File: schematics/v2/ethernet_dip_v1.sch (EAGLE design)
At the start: 30 parts

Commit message: added eeprom
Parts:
- added IC2: DS2432P, 1wire:DS2432P
- added R10: (no value), rcl:R-EU_R0805
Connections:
- net GND: now also IC2P.GND
- net LD2: now also IC2_1W.1W, R10.1
- net VDD: now also R10.2
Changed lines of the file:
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@@
 <part name="GND11" library="supply1" deviceset="GND" device=""/>
 <part name="SUPPLY6" library="SparkFun-Aesthetics" deviceset="VDD" device="" value="+3.3v"/>
+<part name="IC2" library="1wire" deviceset="DS2432" device="P"/>
+<part name="GND14" library="supply1" deviceset="GND" device=""/>
+<part name="R10" library="rcl" deviceset="R-EU_" device="R0805"/>
+<part name="SUPPLY7" library="SparkFun-Aesthetics" deviceset="VDD" device="" value="+3.3v"/>
 </parts>
 <sheets>
@@
 <instance part="GND11" gate="1" x="247.65" y="209.55"/>
 <instance part="SUPPLY6" gate="VDD" x="279.4" y="215.9"/>
+<instance part="IC2" gate="G$1" x="304.8" y="127"/>
+<instance part="IC2" gate="P" x="312.42" y="116.84" rot="R270"/>
+<instance part="IC2" gate="_1W" x="309.88" y="119.38"/>
+<instance part="GND14" gate="1" x="302.26" y="111.76"/>
+<instance part="R10" gate="G$1" x="289.56" y="127" rot="R90"/>
+<instance part="SUPPLY7" gate="VDD" x="289.56" y="134.62"/>
 </instances>
 <busses>
@@
 <wire x1="241.3" y1="213.36" x2="241.3" y2="205.74" width="0.1524" layer="91"/>
 </segment>
+<segment>
+<pinref part="IC2" gate="P" pin="GND"/>
+<pinref part="GND14" gate="1" pin="GND"/>
+<wire x1="304.8" y1="116.84" x2="302.26" y2="116.84" width="0.1524" layer="91"/>
+<wire x1="302.26" y1="116.84" x2="302.26" y2="114.3" width="0.1524" layer="91"/>
+</segment>
 </net>
 <net name="INT0" class="0">
@@
 <wire x1="299.72" y1="198.12" x2="287.02" y2="198.12" width="0.1524" layer="91"/>
 <label x="289.56" y="198.12" size="1.778" layer="95"/>
+</segment>
+<segment>
+<pinref part="IC2" gate="_1W" pin="1W"/>
+<label x="294.64" y="119.38" size="1.778" layer="95"/>
+<wire x1="304.8" y1="119.38" x2="289.56" y2="119.38" width="0.1524" layer="91"/>
+<pinref part="R10" gate="G$1" pin="1"/>
+<wire x1="289.56" y1="119.38" x2="284.48" y2="119.38" width="0.1524" layer="91"/>
+<wire x1="289.56" y1="121.92" x2="289.56" y2="119.38" width="0.1524" layer="91"/>
+<junction x="289.56" y="119.38"/>
 </segment>
 </net>
@@
 <wire x1="279.4" y1="213.36" x2="279.4" y2="215.9" width="0.1524" layer="91"/>
 </segment>
-</net>
+<segment>
+<pinref part="R10" gate="G$1" pin="2"/>
+<wire x1="289.56" y1="134.62" x2="289.56" y2="132.08" width="0.1524" layer="91"/>
+<pinref part="SUPPLY7" gate="VDD" pin="VDD"/>
+</segment>
+</net>

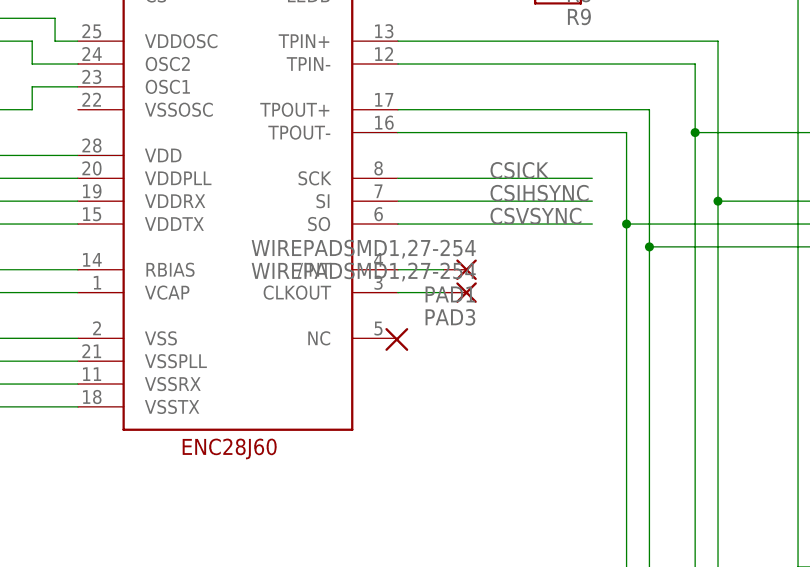
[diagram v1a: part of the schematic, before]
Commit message: routed interrupt pin
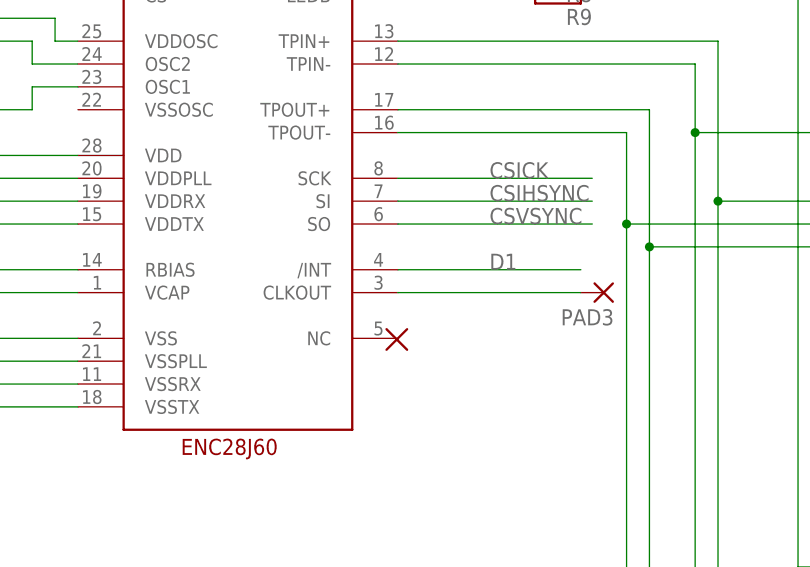
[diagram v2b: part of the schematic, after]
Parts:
- removed PAD1: WIREPADSMD1,27-254, wirepad:WIREPADSMD1,27-254
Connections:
- removed net N$12: PAD1.P, U1./INT
- net D1: now also U1./INT
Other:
- moved on the sheet: PAD3
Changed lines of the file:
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@@
 <part name="C8" library="rcl" deviceset="C-EU" device="C0805"/>
 <part name="GND3" library="supply1" deviceset="GND" device=""/>
-<part name="PAD1" library="wirepad" deviceset="WIREPAD" device="SMD1,27-254"/>
 <part name="PAD3" library="wirepad" deviceset="WIREPAD" device="SMD1,27-254"/>
 <part name="R4" library="rcl" deviceset="R-EU_" device="R0805"/>
@@
 <instance part="C8" gate="G$1" x="41.91" y="165.1" rot="R180"/>
 <instance part="GND3" gate="1" x="241.3" y="139.7"/>
-<instance part="PAD1" gate="G$1" x="116.84" y="172.72" rot="R180"/>
-<instance part="PAD3" gate="G$1" x="116.84" y="170.18" rot="R180"/>
+<instance part="PAD3" gate="G$1" x="132.08" y="170.18" smashed="yes" rot="R180">
+<attribute name="NAME" x="133.223" y="168.3258" size="1.778" layer="95" rot="R180"/>
+</instance>
 <instance part="R4" gate="G$1" x="125.73" y="138.43" rot="R180"/>
 <instance part="R5" gate="G$1" x="125.73" y="134.62" rot="R180"/>
@@
 <label x="388.62" y="180.34" size="1.778" layer="95"/>
 </segment>
+<segment>
+<pinref part="U1" gate="G$1" pin="/INT"/>
+<wire x1="109.22" y1="172.72" x2="129.54" y2="172.72" width="0.1524" layer="91"/>
+<label x="119.38" y="172.72" size="1.778" layer="95"/>
+</segment>
 </net>
 <net name="D3" class="0">
@@
 </segment>
 </net>
-<net name="N$12" class="0">
-<segment>
-<pinref part="U1" gate="G$1" pin="/INT"/>
-<pinref part="PAD1" gate="G$1" pin="P"/>
-<wire x1="114.3" y1="172.72" x2="109.22" y2="172.72" width="0.1524" layer="91"/>
-</segment>
-</net>
 <net name="N$13" class="0">
 <segment>
 <pinref part="U1" gate="G$1" pin="CLKOUT"/>
 <pinref part="PAD3" gate="G$1" pin="P"/>
-<wire x1="114.3" y1="170.18" x2="109.22" y2="170.18" width="0.1524" layer="91"/>
-</segment>
-</net>
+<wire x1="129.54" y1="170.18" x2="109.22" y2="170.18" width="0.1524" layer="91"/>
+</segment>
+</net>
